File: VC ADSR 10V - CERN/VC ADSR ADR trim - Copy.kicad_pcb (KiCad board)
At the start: 2 copper layers, 30 x 18 mm, 40 parts, among them P1 CONN_10, Q1 2N3904, Q2 DMMT3904, Q3 DMMT3906, T1 10K, T2 10K, U1 CD4052, U2 NE555, U3 TL074-

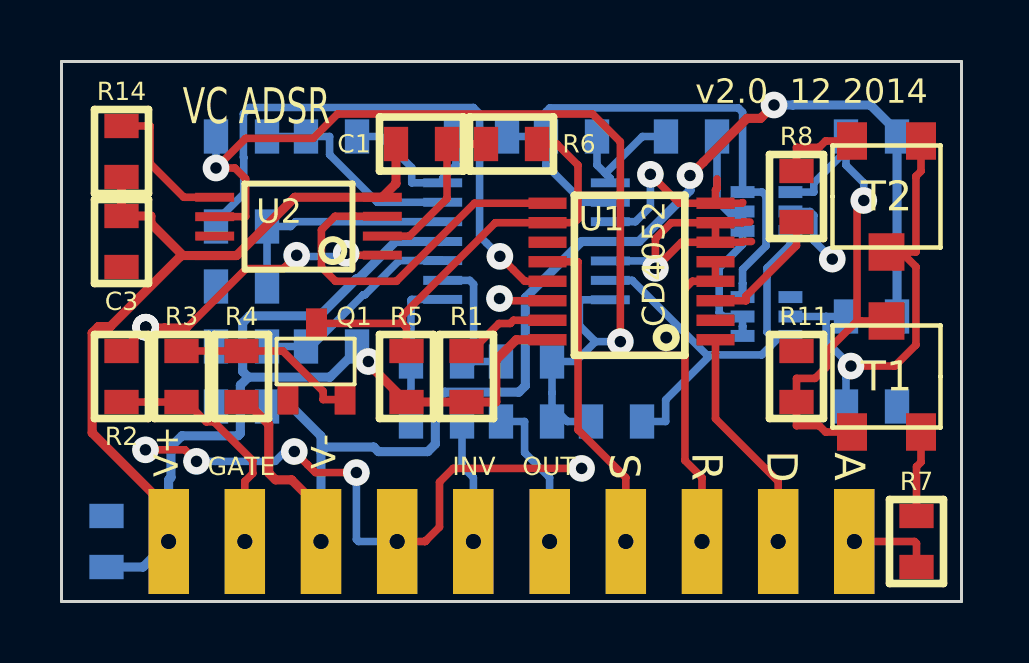
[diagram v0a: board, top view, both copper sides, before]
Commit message: changed Q1 footprint E and B were swapped
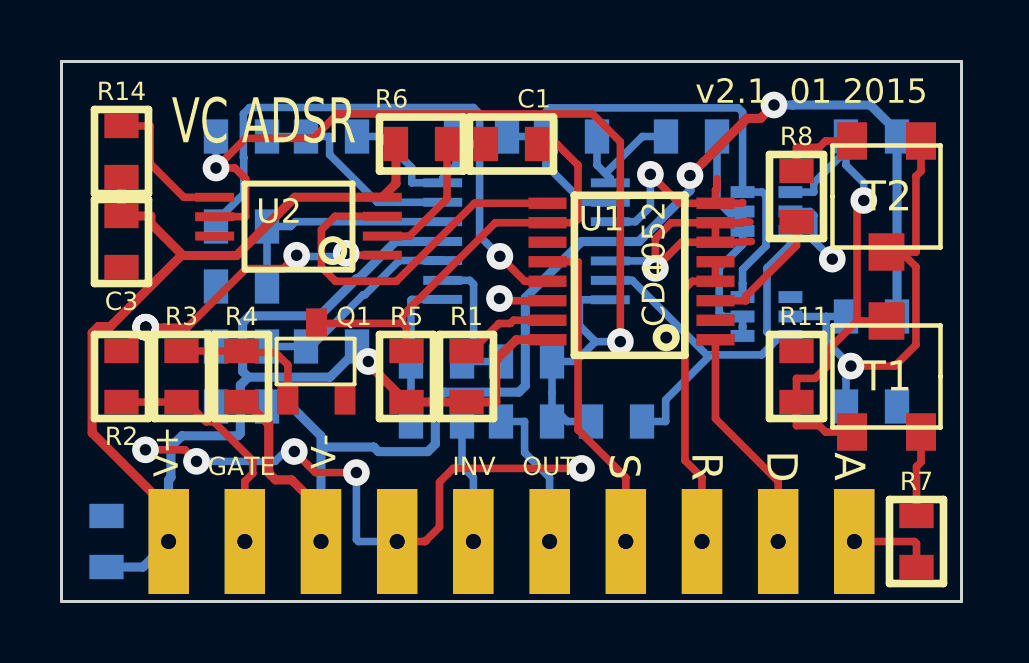
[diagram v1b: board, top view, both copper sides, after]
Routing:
- net N-000001: track 6.28 -> 5.04 mm
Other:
- board text added: "v2.1 01 2015"
- board text removed: "v2.0 12 2014"
